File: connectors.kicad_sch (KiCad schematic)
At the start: 4 parts, among them J1 Conn_01x04_Pin, J2 Conn_01x04_Pin, J3 Conn_01x09_Pin, J4 Conn_02x03_Odd_Even

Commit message: Completed symbol to footprint associations
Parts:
- J1, J2: footprint (none) -> Connector_PinHeader_2.54mm:PinHeader_1x04_P2.54mm_Vertical
- J3: footprint (none) -> Connector_PinHeader_2.54mm:PinHeader_1x09_P2.54mm_Vertical
- J4: footprint (none) -> Connector_PinHeader_2.54mm:PinHeader_2x03_P2.54mm_Vertical
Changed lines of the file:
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@@
 			)
 		)
-		(property "Footprint" ""
+		(property "Footprint" "Connector_PinHeader_2.54mm:PinHeader_1x04_P2.54mm_Vertical"
 			(at 45.72 48.26 0)
 			(effects
@@
 			)
 		)
-		(property "Footprint" ""
+		(property "Footprint" "Connector_PinHeader_2.54mm:PinHeader_2x03_P2.54mm_Vertical"
 			(at 106.68 49.53 0)
 			(effects
@@
 			)
 		)
-		(property "Footprint" ""
+		(property "Footprint" "Connector_PinHeader_2.54mm:PinHeader_1x09_P2.54mm_Vertical"
 			(at 83.82 55.88 0)
 			(effects
@@
 			)
 		)
-		(property "Footprint" ""
+		(property "Footprint" "Connector_PinHeader_2.54mm:PinHeader_1x04_P2.54mm_Vertical"
 			(at 64.77 48.26 0)
 			(effects

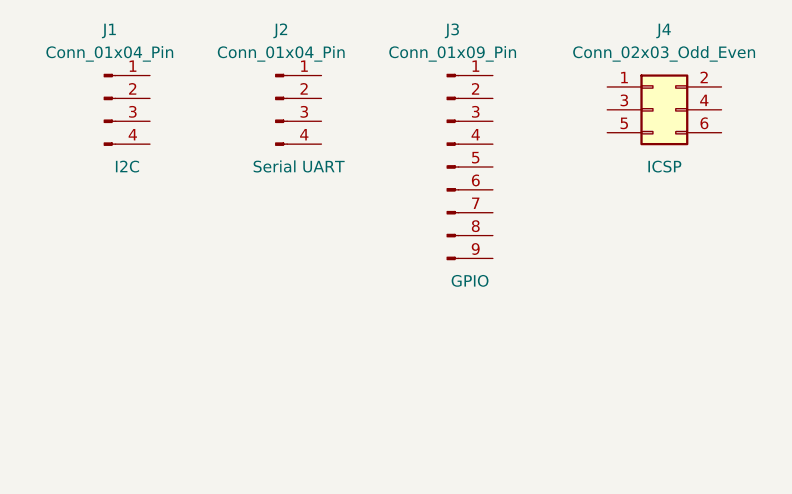
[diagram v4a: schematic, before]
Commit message: Completed wiring in the second sheet
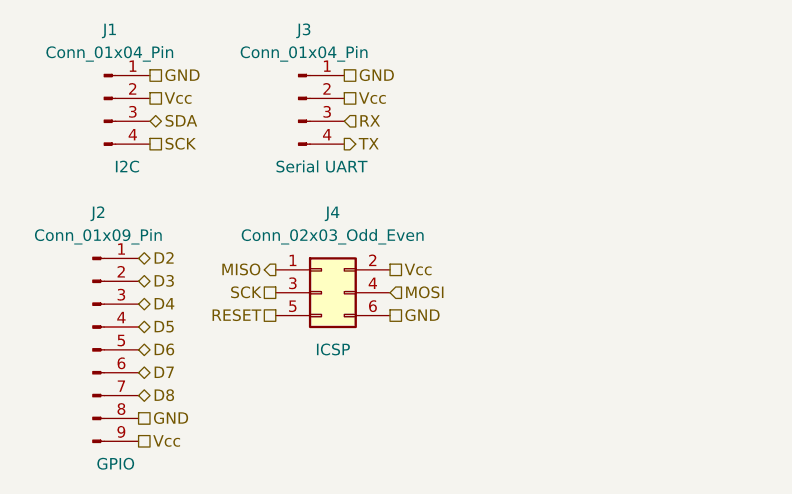
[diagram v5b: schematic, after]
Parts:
- renumbered J3 to J2, J2 to J3
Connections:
- net GND: now reaches J1.1 (Pin_1)
- net GND: now also J2.8 (Pin_8), J3.1 (Pin_1), J4.6 (Pin_6)
- net Vcc: now reaches J1.2 (Pin_2)
- net Vcc: now also J2.9 (Pin_9), J3.2 (Pin_2), J4.2 (Pin_2)
- net SDA: now reaches J1.3 (Pin_3)
- net SCK: now reaches J1.4 (Pin_4)
- net SCK: now also J4.3 (Pin_3)
- net MISO: now reaches J4.1 (Pin_1)
- net MOSI: now reaches J4.4 (Pin_4)
- net RESET: now reaches J4.5 (Pin_5)
- net D2: now reaches J2.1 (Pin_1)
- net D3: now reaches J2.2 (Pin_2)
- net D4: now reaches J2.3 (Pin_3)
- net D5: now reaches J2.4 (Pin_4)
- net D6: now reaches J2.5 (Pin_5)
- net D7: now reaches J2.6 (Pin_6)
- net D8: now reaches J2.7 (Pin_7)
- net RX: now reaches J3.3 (Pin_3)
- net TX: now reaches J3.4 (Pin_4)
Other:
- moved on the sheet: J2, J3, J4
